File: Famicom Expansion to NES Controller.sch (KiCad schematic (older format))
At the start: 3 parts, among them J1 DB15_Female, J2 Conn_01x07_Female, J3 Conn_01x07_Female

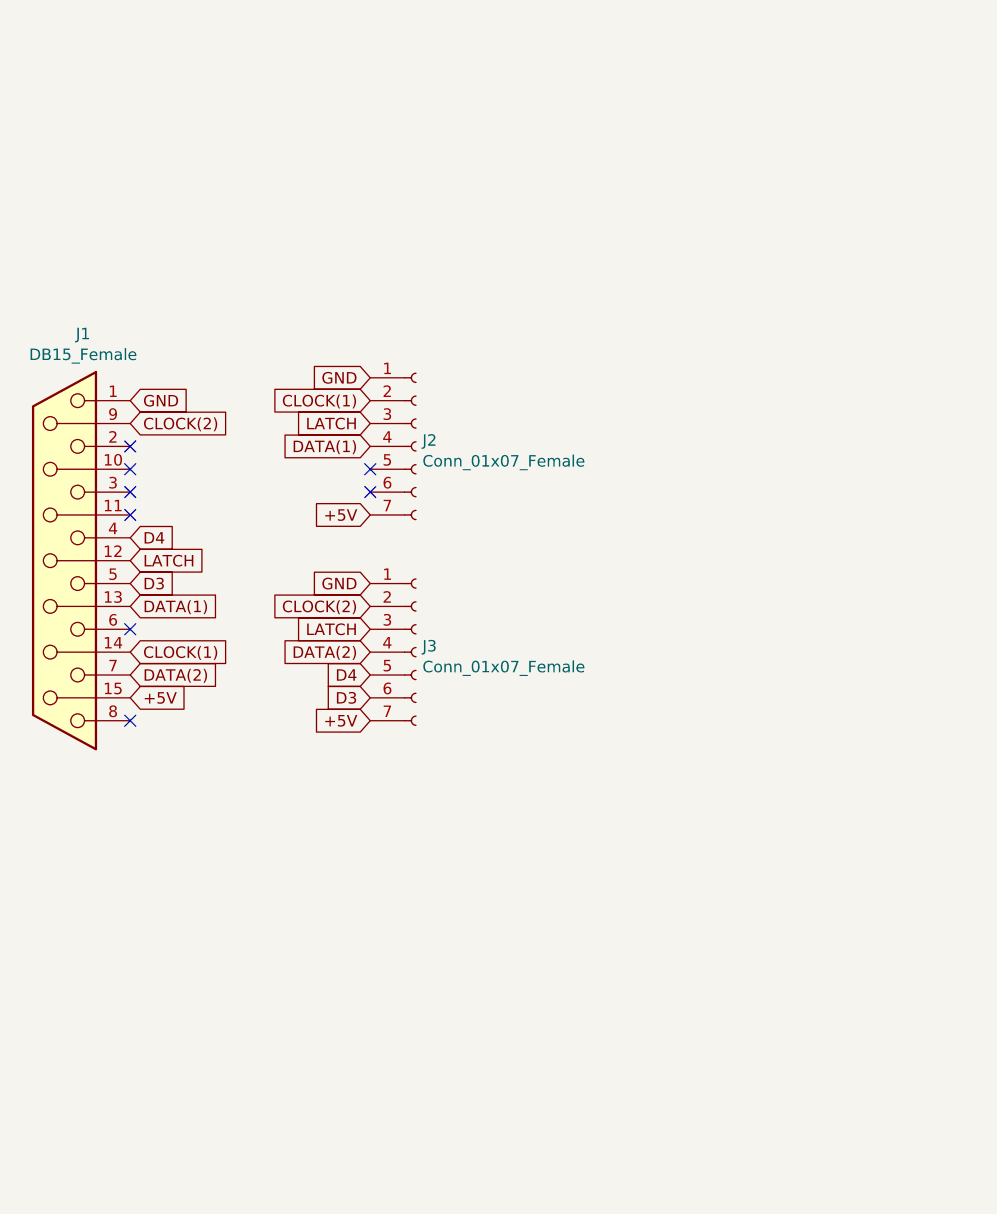
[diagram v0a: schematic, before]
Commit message: Added HDMI Ports for Blissbox compatibility
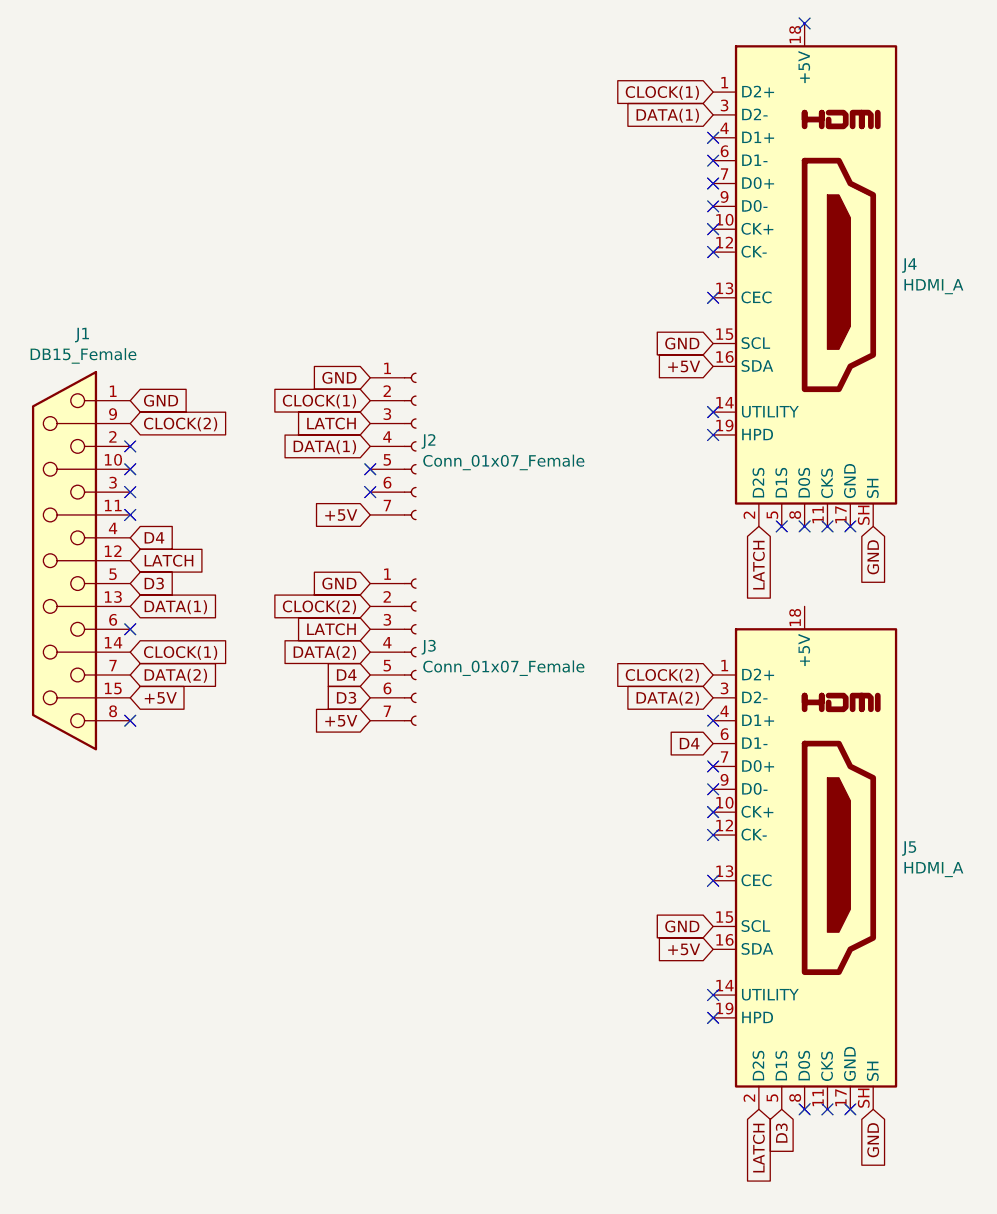
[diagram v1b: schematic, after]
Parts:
- added J4, J5: HDMI_A, Tinkerplunk:HDMI_VERT_47659-1000, symbol Connector:HDMI_A
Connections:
- net +5V: now also J4.16 (SDA), J5.16 (SDA)
- net CLOCK(1): now also J4.1 (D2+)
- net CLOCK(2): now also J5.1 (D2+)
- net D3: now also J5.5 (D1S)
- net D4: now also J5.6 (D1-)
- net DATA(1): now also J4.3 (D2-)
- net DATA(2): now also J5.3 (D2-)
- net GND: now also J4.15 (SCL), J4.SH, J5.15 (SCL), J5.SH
- net LATCH: now also J4.2 (D2S), J5.2 (D2S)
- no-connect marks 8 -> 33
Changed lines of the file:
@@
 NoConn ~ 4950 3550
 NoConn ~ 4950 3950
+$Comp
+L Connector:HDMI_A J5
+U 1 1 5D58C33C
+P 7900 4550
+F 0 "J5" H 8330 4596 50  0000 L CNN
+F 1 "HDMI_A" H 8330 4505 50  0000 L CNN
+F 2 "Tinkerplunk:HDMI_VERT_47659-1000" H 7925 4550 50  0001 C CNN
+F 3 "https://en.wikipedia.org/wiki/HDMI" H 7925 4550 50  0001 C CNN
+	1    7900 4550
+	1    0    0    -1
+$EndComp
+Text GLabel 7500 4850 0    50   Input ~ 0
+GND
+Text GLabel 7500 3750 0    50   Input ~ 0
+CLOCK(2)
+Text GLabel 7700 5650 3    50   Input ~ 0
+LATCH
+Text GLabel 7500 4950 0    50   Input ~ 0
++5V
+Text GLabel 7800 5650 3    50   Input ~ 0
+D3
+Text GLabel 7500 4050 0    50   Input ~ 0
+D4
+$Comp
+L Connector:HDMI_A J4
+U 1 1 5D59042D
+P 7900 2000
+F 0 "J4" H 8330 2046 50  0000 L CNN
+F 1 "HDMI_A" H 8330 1955 50  0000 L CNN
+F 2 "Tinkerplunk:HDMI_VERT_47659-1000" H 7925 2000 50  0001 C CNN
+F 3 "https://en.wikipedia.org/wiki/HDMI" H 7925 2000 50  0001 C CNN
+	1    7900 2000
+	1    0    0    -1
+$EndComp
+Text GLabel 7500 1200 0    50   Input ~ 0
+CLOCK(1)
+Text GLabel 7500 3850 0    50   Input ~ 0
+DATA(2)
+Text GLabel 7500 1300 0    50   Input ~ 0
+DATA(1)
+Text GLabel 7500 2400 0    50   Input ~ 0
++5V
+Text GLabel 7500 2300 0    50   Input ~ 0
+GND
+Text GLabel 8200 3100 3    50   Input ~ 0
+GND
+Text GLabel 8200 5650 3    50   Input ~ 0
+GND
+Text GLabel 7700 3100 3    50   Input ~ 0
+LATCH
+NoConn ~ 7900 900
+NoConn ~ 7500 1400
+NoConn ~ 7500 1500
+NoConn ~ 7500 1600
+NoConn ~ 7500 1700
+NoConn ~ 7500 1800
+NoConn ~ 7500 1900
+NoConn ~ 7500 2100
+NoConn ~ 7500 2600
+NoConn ~ 7500 2700
+NoConn ~ 7800 3100
+NoConn ~ 7900 3100
+NoConn ~ 8000 3100
+NoConn ~ 8100 3100
+NoConn ~ 7500 3950
+NoConn ~ 7500 4150
+NoConn ~ 7500 4250
+NoConn ~ 7500 4350
+NoConn ~ 7500 4450
+NoConn ~ 7500 4650
+NoConn ~ 7500 5150
+NoConn ~ 7500 5250
+NoConn ~ 7900 5650
+NoConn ~ 8000 5650
+NoConn ~ 8100 5650
 $EndSCHEMATC
